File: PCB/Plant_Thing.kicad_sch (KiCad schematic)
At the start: 26 parts, among them U1 nRF52820-QDxx, Y1 32M, Y2 32.768kHz

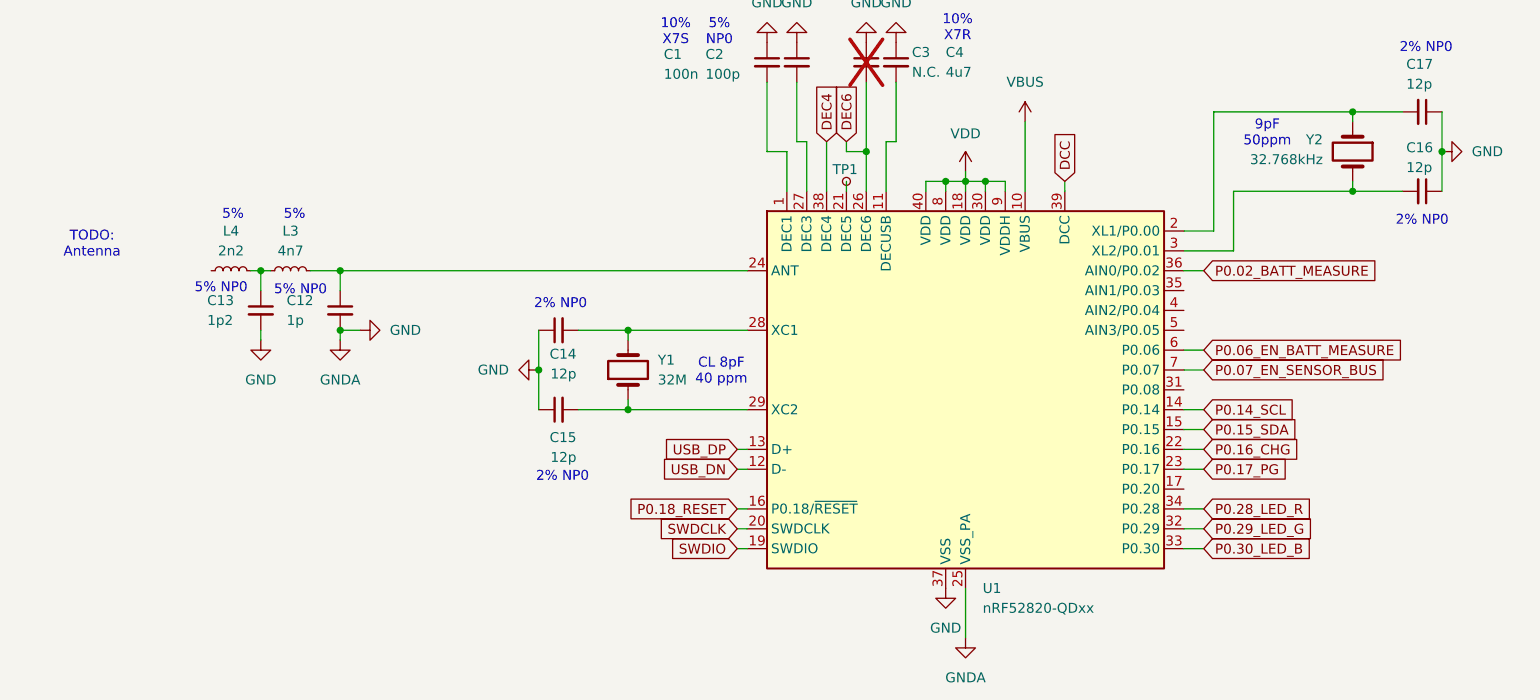
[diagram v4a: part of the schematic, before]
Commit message: added dcdc for external components. Changed board edge to a rect for easier dev board routuing.
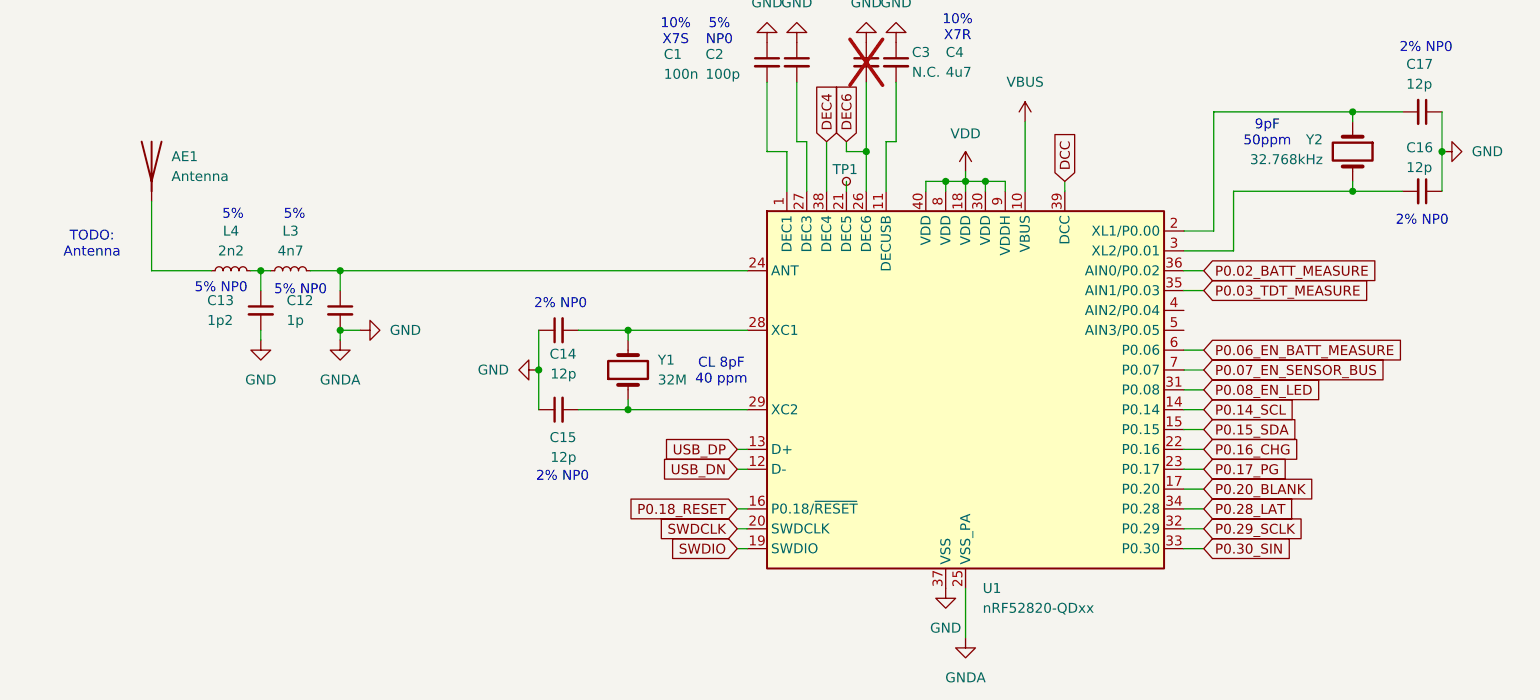
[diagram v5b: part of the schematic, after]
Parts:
- added AE1: Antenna, RF_Antenna:Texas_SWRA117D_2.4GHz_Right, symbol Device:Antenna
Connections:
- net at L4.1: now also AE1.1 (A)
- net P0.20_BLANK: now reaches U1.17 (P0.20)
- net P0.08_EN_LED: now reaches U1.31 (P0.08)
- net P0.03_TDT_MEASURE: now reaches U1.35 (AIN1/P0.03)
- net P0.28_LED_R renamed P0.28_LAT
- net P0.29_LED_G renamed P0.29_SCLK
- net P0.30_LED_B renamed P0.30_SIN
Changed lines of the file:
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@@
 	(wire
 		(pts
+			(xy 45.72 96.52) (xy 45.72 87.63)
+		)
+		(stroke
+			(width 0)
+			(type default)
+		)
+	)
+	(wire
+		(pts
+			(xy 177.8 124.46) (xy 180.34 124.46)
+		)
+		(stroke
+			(width 0)
+			(type default)
+		)
+	)
+	(wire
+		(pts
 			(xy 59.69 104.14) (xy 59.69 105.41)
 		)
@@
 	(wire
 		(pts
+			(xy 177.8 99.06) (xy 180.34 99.06)
+		)
+		(stroke
+			(width 0)
+			(type default)
+		)
+	)
+	(wire
+		(pts
 			(xy 144.78 85.09) (xy 147.32 85.09)
 		)
@@
 	(wire
 		(pts
+			(xy 177.8 111.76) (xy 180.34 111.76)
+		)
+		(stroke
+			(width 0)
+			(type default)
+		)
+	)
+	(wire
+		(pts
 			(xy 199.39 77.47) (xy 199.39 76.2)
 		)
@@
 	(wire
 		(pts
+			(xy 53.34 96.52) (xy 45.72 96.52)
+		)
+		(stroke
+			(width 0)
+			(type default)
+		)
+	)
+	(wire
+		(pts
 			(xy 107.95 34.29) (xy 111.76 34.29)
 		)
@@
 		)
 	)
+	(global_label "P0.08_EN_LED"
+		(shape input)
+		(at 180.34 111.76 0)
+		(fields_autoplaced yes)
+		(effects
+			(font
+				(size 1.27 1.27)
+			)
+			(justify left)
+		)
+		(property "Intersheetrefs" "${INTERSHEET_REFS}"
+			(at 196.6903 111.76 0)
+			(effects
+				(font
+					(size 1.27 1.27)
+				)
+				(justify left)
+				(hide yes)
+			)
+		)
+	)
 	(global_label "DEC6"
 		(shape input)
@@
 		)
 	)
+	(global_label "P0.20_BLANK"
+		(shape input)
+		(at 180.34 124.46 0)
+		(fields_autoplaced yes)
+		(effects
+			(font
+				(size 1.27 1.27)
+			)
+			(justify left)
+		)
+		(property "Intersheetrefs" "${INTERSHEET_REFS}"
+			(at 195.7833 124.46 0)
+			(effects
+				(font
+					(size 1.27 1.27)
+				)
+				(justify left)
+				(hide yes)
+			)
+		)
+	)
 	(global_label "DEC4"
 		(shape input)
@@
 		)
 	)
-	(global_label "P0.28_LED_R"
+	(global_label "P0.06_EN_BATT_MEASURE"
 		(shape input)
-		(at 180.34 127 0)
+		(at 180.34 106.68 0)
 		(fields_autoplaced yes)
 		(effects
@@
 		)
 		(property "Intersheetrefs" "${INTERSHEET_REFS}"
-			(at 195.4808 127 0)
+			(at 207.1526 106.68 0)
 			(effects
 				(font
@@
 		)
 	)
-	(global_label "P0.06_EN_BATT_MEASURE"
+	(global_label "P0.29_SCLK"
 		(shape input)
-		(at 180.34 106.68 0)
+		(at 180.34 129.54 0)
 		(fields_autoplaced yes)
 		(effects
@@
 		)
 		(property "Intersheetrefs" "${INTERSHEET_REFS}"
-			(at 207.1526 106.68 0)
+			(at 194.5737 129.54 0)
 			(effects
 				(font
@@
 		)
 	)
-	(global_label "P0.29_LED_G"
-		(shape input)
-		(at 180.34 129.54 0)
-		(fields_autoplaced yes)
-		(effects
-			(font
-				(size 1.27 1.27)
-			)
-			(justify left)
-		)
-		(property "Intersheetrefs" "${INTERSHEET_REFS}"
-			(at 195.4808 129.54 0)
-			(effects
-				(font
-					(size 1.27 1.27)
-				)
-				(justify left)
-				(hide yes)
-			)
-		)
-	)
 	(global_label "P0.17_PG"
 		(shape input)
@@
 		)
 	)
-	(global_label "P0.30_LED_B"
+	(global_label "P0.30_SIN"
 		(shape input)
 		(at 180.34 132.08 0)
@@
 		)
 		(property "Intersheetrefs" "${INTERSHEET_REFS}"
-			(at 195.4808 132.08 0)
+			(at 192.9409 132.08 0)
 			(effects
 				(font
@@
 		)
 	)
+	(global_label "P0.28_LAT"
+		(shape input)
+		(at 180.34 127 0)
+		(fields_autoplaced yes)
+		(effects
+			(font
+				(size 1.27 1.27)
+			)
+			(justify left)
+		)
+		(property "Intersheetrefs" "${INTERSHEET_REFS}"
+			(at 192.8804 127 0)
+			(effects
+				(font
+					(size 1.27 1.27)
+				)
+				(justify left)
+				(hide yes)
+			)
+		)
+	)
+	(global_label "P0.03_TDT_MEASURE"
+		(shape input)
+		(at 180.34 99.06 0)
+		(fields_autoplaced yes)
+		(effects
+			(font
+				(size 1.27 1.27)
+			)
+			(justify left)
+		)
+		(property "Intersheetrefs" "${INTERSHEET_REFS}"
+			(at 202.6169 99.06 0)
+			(effects
+				(font
+					(size 1.27 1.27)
+				)
+				(justify left)
+				(hide yes)
+			)
+		)
+	)
 	(global_label "DEC6"
 		(shape input)
@@
 					(unit 1)
 				)
+			)
+		)
+	)
+	(symbol
+		(lib_id "Device:Antenna")
+		(at 45.72 82.55 0)
+		(unit 1)
+		(exclude_from_sim no)
+		(in_bom yes)
+		(on_board yes)
+		(dnp no)
+		(fields_autoplaced yes)
+		(property "Reference" "AE1"
+			(at 48.26 81.9149 0)
+			(effects
+				(font
+					(size 1.27 1.27)
+				)
+				(justify left)
+			)
+		)
+		(property "Value" "Antenna"
+			(at 48.26 84.4549 0)
+			(effects
+				(font
+					(size 1.27 1.27)
+				)
+				(justify left)
+			)
+		)
+		(property "Footprint" "RF_Antenna:Texas_SWRA117D_2.4GHz_Right"
+			(at 45.72 82.55 0)
+			(effects
+				(font
+					(size 1.27 1.27)
+				)
+				(hide yes)
+			)
+		)
+		(property "Datasheet" "~"
+			(at 45.72 82.55 0)
+			(effects
+				(font
+					(size 1.27 1.27)
+				)
+				(hide yes)
+			)
+		)
+		(property "Description" "Antenna"
+			(at 45.72 82.55 0)
+			(effects
+				(font
+					(size 1.27 1.27)
+				)
+				(hide yes)
+			)
+		)
+		(pin "1"
+		)
+		(instances
+			(project "Plant_Thing"
+				(path "/3604ffe7-6852-4862-a71a-75c04c0147cb"
+					(reference "AE1")
+					(unit 1)
+				)

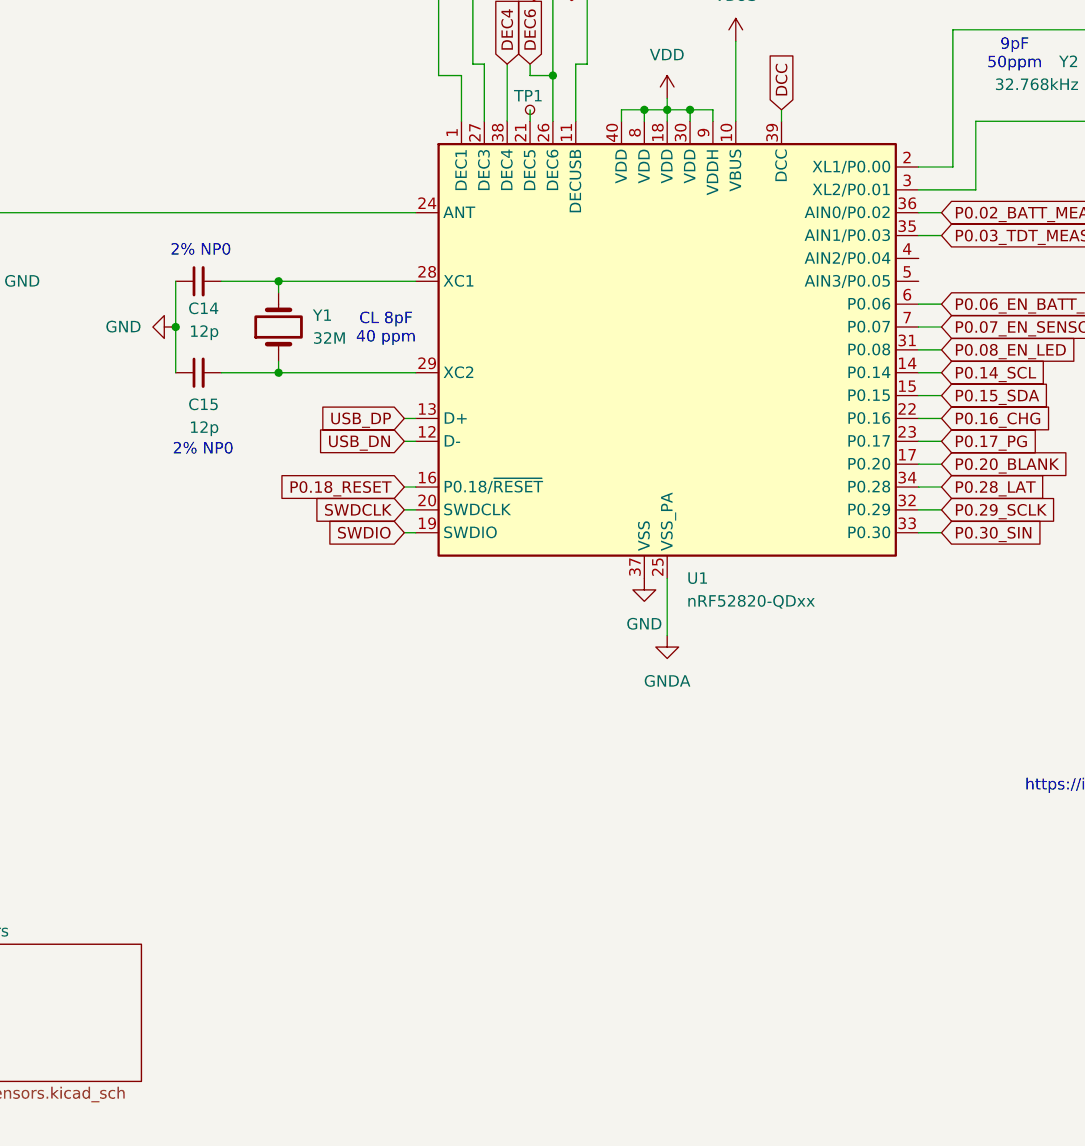
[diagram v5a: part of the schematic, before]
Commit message: redid the pcb layout for a more bigger devboard approach. Added a few more components and the antenna.
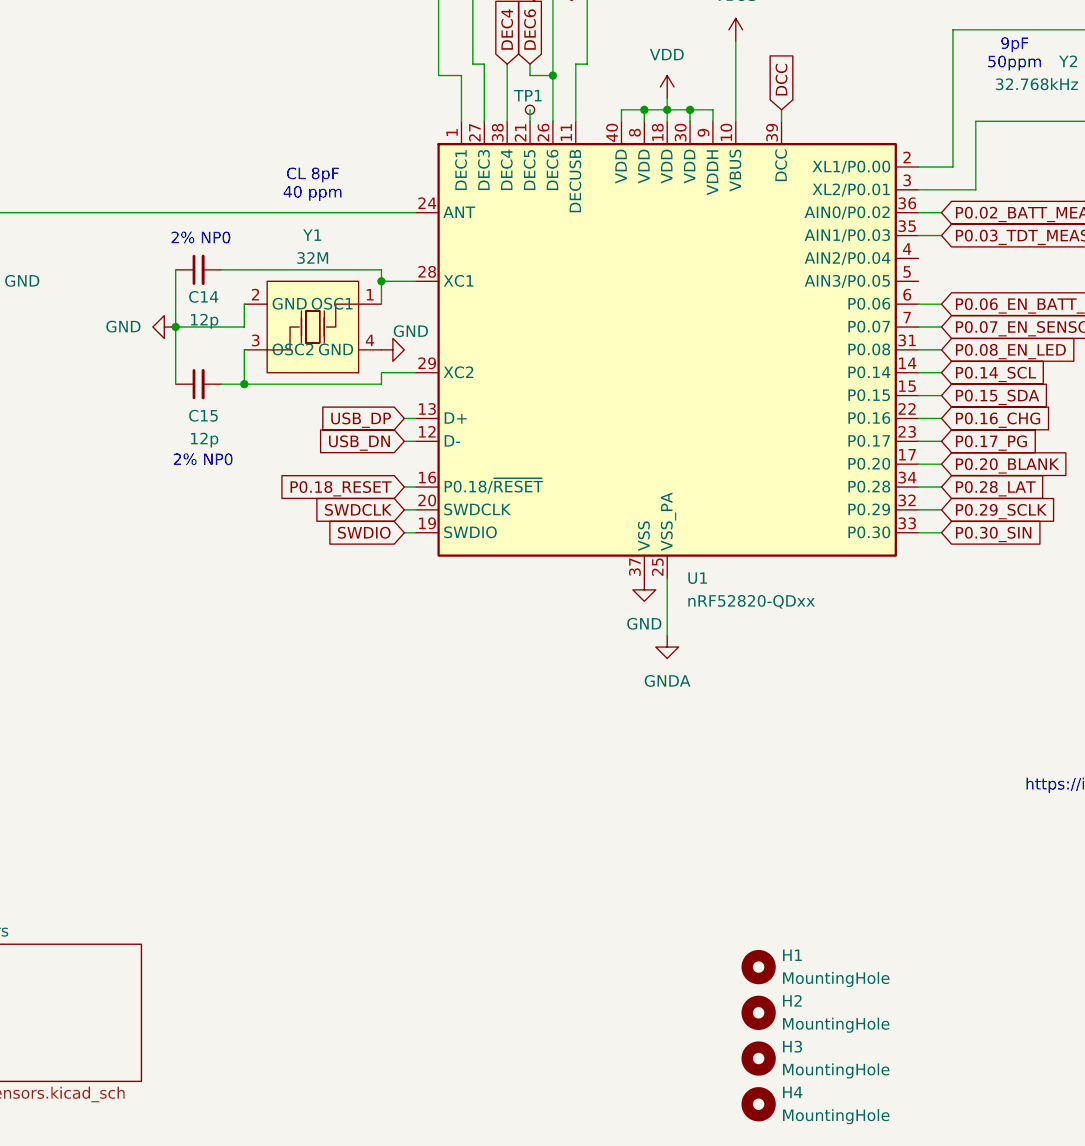
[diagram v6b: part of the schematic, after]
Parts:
- added H1, H2, H3, H4: MountingHole, MountingHole:MountingHole_2.7mm_M2.5_DIN965, symbol Mechanical:MountingHole
- C12, C13: footprint Capacitor_SMD:C_0402_1005Metric -> Capacitor_SMD:C_0201_0603Metric
- L3, L4: footprint Inductor_SMD:L_0402_1005Metric -> Inductor_SMD:L_0201_0603Metric
- Y1: footprint (none) -> X322532MOB4SI:CRYSTAL-SMD_4P-L3.2-W2.5-BL; symbol Device:Crystal -> X322532MOB4SI:X322532MOB4SI; LCSC Part (none) -> C9009
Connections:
- net GND: now also Y1.2 (GND), Y1.4 (GND)
- net at C15.2, U1.29 (XC2): now also Y1.3 (OSC2); no longer Y1.1
- net at C14.2, U1.28 (XC1): now also Y1.1 (OSC1); no longer Y1.2
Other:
- moved on the sheet: C14, C15

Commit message: Added more Components
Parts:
- removed Y2: 32.768kHz, symbol Device:Crystal
- added J7: VDDH, Connector_PinHeader_2.54mm:PinHeader_1x02_P2.54mm_Vertical, symbol Connector:Conn_01x02_Pin
- added J8: EXT 3.3V, Connector_PinHeader_2.54mm:PinHeader_1x02_P2.54mm_Vertical, symbol Connector:Conn_01x02_Pin
- added JP3: SolderJumper_3_Bridged12, Jumper:SolderJumper-3_P1.3mm_Bridged12_RoundedPad1.0x1.5mm, symbol Jumper:SolderJumper_3_Bridged12
- added X1: HY32768KSMD3068YA2R30, HY32768KSMD3068YA2R30:CRYSTAL-SMD_L7.0-W3.2-LS7.5, symbol HY32768KSMD3068YA2R30:HY32768KSMD3068YA2R30
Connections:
- net GND: now also J8.1 (Pin_1)
- net VDD: now also J8.2 (Pin_2), JP3.3 (B); no longer U1.9 (VDDH)
- net at C17.2, U1.2 (XL1/P0.00): now also X1.2
- net at C16.2, U1.3 (XL2/P0.01): now also X1.1
- net P0.04_AGPIO: now reaches U1.4 (AIN2/P0.04)
- net P0.05_EN_DCDC: now reaches U1.5 (AIN3/P0.05)
- new net: J7.1 (Pin_1), JP3.1 (A)
- new net VCC: JP3.2 (C)
- new net VDDH: J7.2 (Pin_2), U1.9 (VDDH)

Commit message: Continued on Devboard
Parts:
- removed AE1: Antenna, RF_Antenna:Texas_SWRA117D_2.4GHz_Right, symbol Device:Antenna
- added AE1: Antenna_Shield, RF_Antenna:Texas_SWRA117D_2.4GHz_Left, symbol Device:Antenna_Shield
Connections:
- net GND: now also AE1.2 (Shield)
- net at L4.1: now also AE1.1 (A)
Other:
- note added: "TODO RESET BUTTON"
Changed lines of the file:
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@@
 	(wire
 		(pts
-			(xy 45.72 96.52) (xy 45.72 87.63)
-		)
-		(stroke
-			(width 0)
-			(type default)
-		)
-	)
-	(wire
-		(pts
 			(xy 102.87 109.22) (xy 95.25 109.22)
 		)
@@
 		)
 	)
+	(text "TODO\nRESET BUTTON"
+		(exclude_from_sim no)
+		(at 103.886 141.478 0)
+		(effects
+			(font
+				(size 1.27 1.27)
+			)
+		)
+	)
 	(text "5% NP0"
 		(exclude_from_sim no)
@@
 	(symbol
 		(lib_id "power:GND")
+		(at 43.18 96.52 0)
+		(unit 1)
+		(exclude_from_sim no)
+		(in_bom yes)
+		(on_board yes)
+		(dnp no)
+		(fields_autoplaced yes)
+		(property "Reference" "#PWR073"
+			(at 43.18 102.87 0)
+			(effects
+				(font
+					(size 1.27 1.27)
+				)
+				(hide yes)
+			)
+		)
+		(property "Value" "GND"
+			(at 43.18 101.6 0)
+			(effects
+				(font
+					(size 1.27 1.27)
+				)
+			)
+		)
+		(property "Footprint" ""
+			(at 43.18 96.52 0)
+			(effects
+				(font
+					(size 1.27 1.27)
+				)
+				(hide yes)
+			)
+		)
+		(property "Datasheet" ""
+			(at 43.18 96.52 0)
+			(effects
+				(font
+					(size 1.27 1.27)
+				)
+				(hide yes)
+			)
+		)
+		(property "Description" "Power symbol creates a global label with name \"GND\" , ground"
+			(at 43.18 96.52 0)
+			(effects
+				(font
+					(size 1.27 1.27)
+				)
+				(hide yes)
+			)
+		)
+		(pin "1"
+		)
+		(instances
+			(project "Plant_Thing"
+				(path "/3604ffe7-6852-4862-a71a-75c04c0147cb"
+					(reference "#PWR073")
+					(unit 1)
+				)
+			)
+		)
+	)
+	(symbol
+		(lib_id "power:GND")
 		(at 95.25 109.22 270)
 		(unit 1)
@@
 	)
 	(symbol
-		(lib_id "Device:Antenna")
-		(at 45.72 82.55 0)
-		(unit 1)
-		(exclude_from_sim no)
-		(in_bom yes)
-		(on_board yes)
-		(dnp no)
-		(fields_autoplaced yes)
-		(property "Reference" "AE1"
-			(at 48.26 81.9149 0)
-			(effects
-				(font
-					(size 1.27 1.27)
-				)
-				(justify left)
-			)
-		)
-		(property "Value" "Antenna"
-			(at 48.26 84.4549 0)
-			(effects
-				(font
-					(size 1.27 1.27)
-				)
-				(justify left)
-			)
-		)
-		(property "Footprint" "RF_Antenna:Texas_SWRA117D_2.4GHz_Right"
-			(at 45.72 82.55 0)
-			(effects
-				(font
-					(size 1.27 1.27)
-				)
-				(hide yes)
-			)
-		)
-		(property "Datasheet" "~"
-			(at 45.72 82.55 0)
-			(effects
-				(font
-					(size 1.27 1.27)
-				)
-				(hide yes)
-			)
-		)
-		(property "Description" "Antenna"
-			(at 45.72 82.55 0)
-			(effects
-				(font
-					(size 1.27 1.27)
-				)
-				(hide yes)
-			)
-		)
-		(pin "1"
-		)
-		(instances
-			(project "Plant_Thing"
-				(path "/3604ffe7-6852-4862-a71a-75c04c0147cb"
-					(reference "AE1")
-					(unit 1)
-				)
-			)
-		)
-	)
-	(symbol
 		(lib_id "Device:C_Small")
 		(at 97.79 102.87 90)
@@
 					(unit 1)
 				)
+			)
+		)
+	)
+	(symbol
+		(lib_id "Device:Antenna_Shield")
+		(at 45.72 91.44 0)
+		(mirror y)
+		(unit 1)
+		(exclude_from_sim no)
+		(in_bom yes)
+		(on_board yes)
+		(dnp no)
+		(property "Reference" "AE1"
+			(at 41.91 89.5349 0)
+			(effects
+				(font
+					(size 1.27 1.27)
+				)
+				(justify left)
+			)
+		)
+		(property "Value" "Antenna_Shield"
+			(at 41.91 92.0749 0)
+			(effects
+				(font
+					(size 1.27 1.27)
+				)
+				(justify left)
+			)
+		)
+		(property "Footprint" "RF_Antenna:Texas_SWRA117D_2.4GHz_Left"
+			(at 45.72 88.9 0)
+			(effects
+				(font
+					(size 1.27 1.27)
+				)
+				(hide yes)
+			)
+		)
+		(property "Datasheet" "~"
+			(at 45.72 88.9 0)
+			(effects
+				(font
+					(size 1.27 1.27)
+				)
+				(hide yes)
+			)
+		)
+		(property "Description" "Antenna with extra pin for shielding"
+			(at 45.72 91.44 0)
+			(effects
+				(font
+					(size 1.27 1.27)
+				)
+				(hide yes)
+			)
+		)
+		(pin "1"
+		)
+		(pin "2"
+		)
+		(instances
+			(project "Plant_Thing"
+				(path "/3604ffe7-6852-4862-a71a-75c04c0147cb"
+					(reference "AE1")
+					(unit 1)
+				)
